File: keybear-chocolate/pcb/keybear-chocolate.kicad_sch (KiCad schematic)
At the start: 94 parts, among them J1 MJ-4PP-9, J3 LED, J4 OLED, P1 i2c-pin, P2 i2c-pin, SW1 SW_PUSH, SW10 SW_PUSH, SW11 SW_PUSH, SW12 SW_PUSH, SW13 SW_PUSH, SW14 SW_PUSH, SW15 SW_PUSH, SW16 SW_PUSH, SW17 SW_PUSH, SW18 SW_PUSH, SW19 SW_PUSH, SW2 SW_PUSH, SW20 SW_PUSH, SW21 SW_PUSH, SW22 SW_PUSH, SW23 SW_PUSH, SW25 Rotary_Encoder_Switch, SW3 SW_PUSH, SW4 SW_PUSH, SW5 SW_PUSH, SW6 SW_PUSH, SW7 SW_PUSH, SW8 SW_PUSH, SW9 SW_PUSH, U1 ProMicro

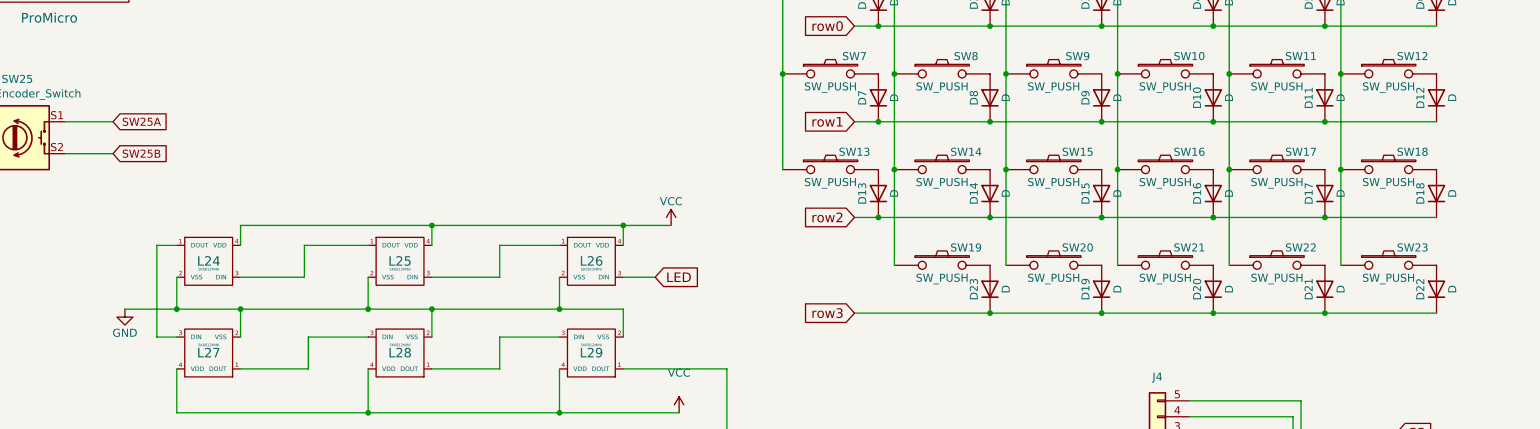
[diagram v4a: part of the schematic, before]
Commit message: rotary button mapped
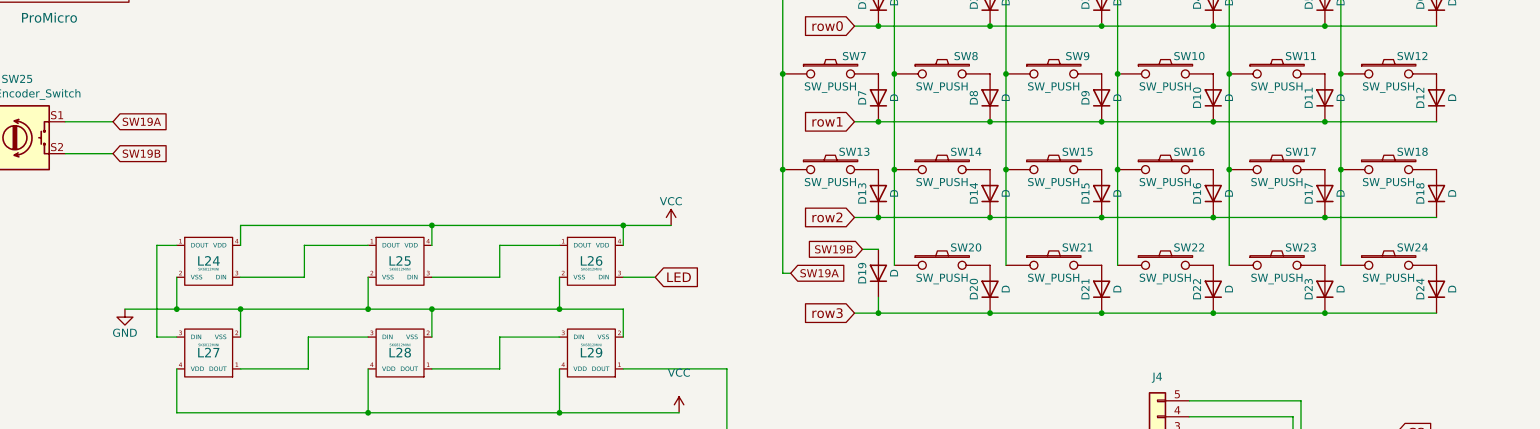
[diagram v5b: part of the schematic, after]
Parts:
- added D19: D, kbd:D3_SMD, symbol Device:D
- renumbered D23 to D20, D19 to D21, D20 to D22, D21 to D23, D22 to D24, SW19 to SW20, SW20 to SW21, SW21 to SW22, SW22 to SW23, SW23 to SW24
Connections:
- net col0 is gone; now on net SW19A: SW1.1, SW13.1, SW7.1, U1.20 (F4)
- net row3: now also D19.1 (K)
- net SW25A renamed SW19A
- net SW25B renamed SW19B
- net SW19B: now also D19.2 (A)
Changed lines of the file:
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@@
   (junction (at 250.19 104.14) (diameter 0) (color 0 0 0 0)
   )
+  (junction (at 179.07 104.14) (diameter 0) (color 0 0 0 0)
+  )
   (junction (at 196.85 73.66) (diameter 0) (color 0 0 0 0)
   )
@@
   (junction (at 200.66 151.765) (diameter 0) (color 0 0 0 0)
   )
+  (junction (at 163.83 81.28) (diameter 0) (color 0 0 0 0)
+  )
   (junction (at 107.95 103.505) (diameter 0) (color 0 0 0 0)
   )
@@
     (stroke (width 0) (type default))
   )
+  (wire (pts (xy 179.07 101.6) (xy 179.07 104.14))
+    (stroke (width 0) (type default))
+  )
   (wire (pts (xy 130.81 182.88) (xy 115.57 182.88))
     (stroke (width 0) (type default))
@@
     (stroke (width 0) (type default))
   )
+  (wire (pts (xy 163.83 97.79) (xy 163.83 81.28))
+    (stroke (width 0) (type default))
+  )
   (wire (pts (xy 74.93 173.99) (xy 74.93 170.18))
     (stroke (width 0) (type default))
@@
     (stroke (width 0) (type default))
   )
+  (wire (pts (xy 179.07 104.14) (xy 196.85 104.14))
+    (stroke (width 0) (type default))
+  )
   (wire (pts (xy 138.43 90.17) (xy 146.05 90.17))
     (stroke (width 0) (type default))
@@
     (stroke (width 0) (type default))
   )
-  (wire (pts (xy 175.26 104.14) (xy 196.85 104.14))
+  (wire (pts (xy 175.26 104.14) (xy 179.07 104.14))
     (stroke (width 0) (type default))
   )
@@
     (stroke (width 0) (type default))
   )
+  (wire (pts (xy 165.1 97.79) (xy 163.83 97.79))
+    (stroke (width 0) (type default))
+  )
   (wire (pts (xy 57.15 166.37) (xy 59.69 166.37))
     (stroke (width 0) (type default))
@@
     (stroke (width 0) (type default))
   )
+  (wire (pts (xy 176.53 93.98) (xy 179.07 93.98))
+    (stroke (width 0) (type default))
+  )
   (wire (pts (xy 77.47 113.03) (xy 88.265 113.03))
     (stroke (width 0) (type default))
@@
     )
   )
+  (global_label "SW19A" (shape input) (at 165.1 97.79 0)
+    (effects (font (size 1.27 1.27)) (justify left))
+    (property "Intersheetrefs" "${INTERSHEET_REFS}" (at 165.1 97.79 0)
+      (effects (font (size 1.27 1.27)) hide)
+    )
+  )
   (global_label "data" (shape input) (at 215.9 151.765 0) (fields_autoplaced)
     (effects (font (size 1.524 1.524)) (justify left))
@@
     )
   )
-  (global_label "SW25B" (shape input) (at 57.15 78.74 0)
+  (global_label "SW19B" (shape input) (at 57.15 78.74 0)
     (effects (font (size 1.27 1.27)) (justify left))
     (property "Intersheetrefs" "${INTERSHEET_REFS}" (at 57.15 78.74 0)
@@
     )
   )
+  (global_label "SW19B" (shape input) (at 176.53 93.98 180)
+    (effects (font (size 1.27 1.27)) (justify right))
+    (property "Intersheetrefs" "${INTERSHEET_REFS}" (at 176.53 93.98 0)
+      (effects (font (size 1.27 1.27)) hide)
+    )
+  )
   (global_label "ENCA" (shape input) (at 30.48 73.66 180)
     (effects (font (size 1.27 1.27)) (justify right))
@@
     )
   )
-  (global_label "SW25A" (shape input) (at 57.15 73.66 0)
+  (global_label "SW19A" (shape input) (at 57.15 73.66 0)
     (effects (font (size 1.27 1.27)) (justify left))
     (property "Intersheetrefs" "${INTERSHEET_REFS}" (at 57.15 73.66 0)
@@
   (symbol (lib_id "corne-chocolate-rescue:SW_PUSH-kbd") (at 242.57 96.52 0) (unit 1)
     (in_bom yes) (on_board yes) (dnp no)
-    (property "Reference" "SW22" (at 246.38 93.726 0)
+    (property "Reference" "SW23" (at 246.38 93.726 0)
       (effects (font (size 1.27 1.27)))
     )
@@
       (project "keybear-chocolate"
         (path "/b2404ab0-025a-473e-9fbb-0abc932972cf"
-          (reference "SW22") (unit 1)
+          (reference "SW23") (unit 1)
         )
       )
@@
   (symbol (lib_id "Device:D") (at 250.19 100.33 90) (unit 1)
     (in_bom yes) (on_board yes) (dnp no)
-    (property "Reference" "D21" (at 247.65 100.33 0)
+    (property "Reference" "D23" (at 247.65 100.33 0)
       (effects (font (size 1.27 1.27)))
     )
@@
       (project "keybear-chocolate"
         (path "/b2404ab0-025a-473e-9fbb-0abc932972cf"
-          (reference "D21") (unit 1)
+          (reference "D23") (unit 1)
         )
       )
@@
   (symbol (lib_id "corne-chocolate-rescue:SW_PUSH-kbd") (at 260.35 96.52 0) (unit 1)
     (in_bom yes) (on_board yes) (dnp no)
-    (property "Reference" "SW23" (at 264.16 93.726 0)
+    (property "Reference" "SW24" (at 264.16 93.726 0)
       (effects (font (size 1.27 1.27)))
     )
@@
       (project "keybear-chocolate"
         (path "/b2404ab0-025a-473e-9fbb-0abc932972cf"
-          (reference "SW23") (unit 1)
+          (reference "SW24") (unit 1)
         )
       )
@@
   (symbol (lib_id "Device:D") (at 267.97 100.33 90) (unit 1)
     (in_bom yes) (on_board yes) (dnp no)
-    (property "Reference" "D22" (at 265.43 100.33 0)
+    (property "Reference" "D24" (at 265.43 100.33 0)
       (effects (font (size 1.27 1.27)))
     )
@@
       (project "keybear-chocolate"
         (path "/b2404ab0-025a-473e-9fbb-0abc932972cf"
-          (reference "D22") (unit 1)
+          (reference "D24") (unit 1)
         )
       )
@@
   (symbol (lib_id "corne-chocolate-rescue:SW_PUSH-kbd") (at 224.79 96.52 0) (unit 1)
     (in_bom yes) (on_board yes) (dnp no)
-    (property "Reference" "SW21" (at 228.6 93.726 0)
+    (property "Reference" "SW22" (at 228.6 93.726 0)
       (effects (font (size 1.27 1.27)))
     )
@@
       (project "keybear-chocolate"
         (path "/b2404ab0-025a-473e-9fbb-0abc932972cf"
-          (reference "SW21") (unit 1)
+          (reference "SW22") (unit 1)
         )
       )
@@
   (symbol (lib_id "Device:D") (at 232.41 100.33 90) (unit 1)
     (in_bom yes) (on_board yes) (dnp no)
-    (property "Reference" "D20" (at 229.87 100.33 0)
+    (property "Reference" "D22" (at 229.87 100.33 0)
       (effects (font (size 1.27 1.27)))
     )
@@
       (project "keybear-chocolate"
         (path "/b2404ab0-025a-473e-9fbb-0abc932972cf"
-          (reference "D20") (unit 1)
+          (reference "D22") (unit 1)
         )
       )
@@
   (symbol (lib_id "corne-chocolate-rescue:SW_PUSH-kbd") (at 189.23 96.52 0) (unit 1)
     (in_bom yes) (on_board yes) (dnp no)
-    (property "Reference" "SW19" (at 193.04 93.726 0)
+    (property "Reference" "SW20" (at 193.04 93.726 0)
       (effects (font (size 1.27 1.27)))
     )
@@
       (project "keybear-chocolate"
         (path "/b2404ab0-025a-473e-9fbb-0abc932972cf"
-          (reference "SW19") (unit 1)
+          (reference "SW20") (unit 1)
         )
       )
@@
     )
   )
+  (symbol (lib_id "Device:D") (at 179.07 97.79 90) (unit 1)
+    (in_bom yes) (on_board yes) (dnp no)
+    (property "Reference" "D19" (at 176.53 97.79 0)
+      (effects (font (size 1.27 1.27)))
+    )
+    (property "Value" "D" (at 181.61 97.79 0)
+      (effects (font (size 1.27 1.27)))
+    )
+    (property "Footprint" "kbd:D3_SMD" (at 179.07 97.79 0)
+      (effects (font (size 1.27 1.27)) hide)
+    )
+    (property "Datasheet" "" (at 179.07 97.79 0)
+      (effects (font (size 1.27 1.27)) hide)
+    )
+    (pin "1")
+    (pin "2")
+    (instances
+      (project "keybear-chocolate"
+        (path "/b2404ab0-025a-473e-9fbb-0abc932972cf"
+          (reference "D19") (unit 1)
+        )
+      )
+    )
+  )
   (symbol (lib_id "SofleKeyboard-rescue:Rotary_Encoder_Switch-Device") (at 41.91 76.2 0) (unit 1)
     (in_bom yes) (on_board yes) (dnp no)
@@
   (symbol (lib_id "Device:D") (at 214.63 100.33 90) (unit 1)
     (in_bom yes) (on_board yes) (dnp no)
-    (property "Reference" "D19" (at 212.09 100.33 0)
+    (property "Reference" "D21" (at 212.09 100.33 0)
       (effects (font (size 1.27 1.27)))
     )
@@
       (project "keybear-chocolate"
         (path "/b2404ab0-025a-473e-9fbb-0abc932972cf"
-          (reference "D19") (unit 1)
+          (reference "D21") (unit 1)
         )
       )
@@
   (symbol (lib_id "corne-chocolate-rescue:SW_PUSH-kbd") (at 207.01 96.52 0) (unit 1)
     (in_bom yes) (on_board yes) (dnp no)
-    (property "Reference" "SW20" (at 210.82 93.726 0)
+    (property "Reference" "SW21" (at 210.82 93.726 0)
       (effects (font (size 1.27 1.27)))
     )
@@
       (project "keybear-chocolate"
         (path "/b2404ab0-025a-473e-9fbb-0abc932972cf"
-          (reference "SW20") (unit 1)
+          (reference "SW21") (unit 1)
         )
       )
@@
   (symbol (lib_id "Device:D") (at 196.85 100.33 90) (unit 1)
     (in_bom yes) (on_board yes) (dnp no)
-    (property "Reference" "D23" (at 194.31 100.33 0)
+    (property "Reference" "D20" (at 194.31 100.33 0)
       (effects (font (size 1.27 1.27)))
     )
@@
       (project "keybear-chocolate"
         (path "/b2404ab0-025a-473e-9fbb-0abc932972cf"
-          (reference "D23") (unit 1)
+          (reference "D20") (unit 1)
         )
       )

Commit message: latest schematics
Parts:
- added J2: BATT, kbd:StripLED_rev, symbol Connector_Generic:Conn_01x02
- added SW30: BATT_SW, Button_Switch_SMD:SW_SPDT_PCM12, symbol Switch:SW_SPDT
- SW1, SW2, SW3, SW4, SW5, SW6: footprint SofleChoc:Choc_Hotswap_SK6812MiniE -> kbd:Choc_Hotswap
- renumbered L19 to L20, L20 to L21, L21 to L22, L22 to L23, L23 to L24, L24 to L25, L25 to L26, L26 to L27, L27 to L28, L28 to L29, L29 to L30
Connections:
- net GND: now also J2.1 (Pin_1)
- net RAW: now reaches U1.24 (RAW)
- net RAW: now also SW30.1 (A)
- new net BATT_VCC: J2.2 (Pin_2), SW30.2 (B)

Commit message: using custom footprints
using custom footprints for leds and oled display
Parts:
- J4: footprint kbd:OLED -> kbd:OLED_xo_5pins
- L1, L10, L11, L12, L13, L14, L15, L16, L17, L18, L2, L20, L21, L22, L23, L24, L25, L26, L27, L28, L29, L3, L30, L4, L5, L6, L7, L8, L9: footprint kbd:SK6812MINI_rev -> kbd:SK6812MINI_xo_rev
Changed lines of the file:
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@@
       (effects (font (size 0.4064 0.4064)))
     )
-    (property "Footprint" "kbd:SK6812MINI_rev" (at 80.01 138.43 0)
+    (property "Footprint" "kbd:SK6812MINI_xo_rev" (at 80.01 138.43 0)
       (effects (font (size 1.524 1.524)) hide)
     )
@@
       (effects (font (size 0.4064 0.4064)))
     )
-    (property "Footprint" "kbd:SK6812MINI_rev" (at 95.25 138.43 0)
+    (property "Footprint" "kbd:SK6812MINI_xo_rev" (at 95.25 138.43 0)
       (effects (font (size 1.524 1.524)) hide)
     )
@@
       (effects (font (size 0.4064 0.4064)))
     )
-    (property "Footprint" "kbd:SK6812MINI_rev" (at 110.49 138.43 0)
+    (property "Footprint" "kbd:SK6812MINI_xo_rev" (at 110.49 138.43 0)
       (effects (font (size 1.524 1.524)) hide)
     )
@@
       (effects (font (size 0.4064 0.4064)))
     )
-    (property "Footprint" "kbd:SK6812MINI_rev" (at 125.73 138.43 0)
+    (property "Footprint" "kbd:SK6812MINI_xo_rev" (at 125.73 138.43 0)
       (effects (font (size 1.524 1.524)) hide)
     )
@@
       (effects (font (size 0.4064 0.4064)))
     )
-    (property "Footprint" "kbd:SK6812MINI_rev" (at 140.97 138.43 0)
+    (property "Footprint" "kbd:SK6812MINI_xo_rev" (at 140.97 138.43 0)
       (effects (font (size 1.524 1.524)) hide)
     )
@@
       (effects (font (size 0.4064 0.4064)))
     )
-    (property "Footprint" "kbd:SK6812MINI_rev" (at 64.77 138.43 0)
+    (property "Footprint" "kbd:SK6812MINI_xo_rev" (at 64.77 138.43 0)
       (effects (font (size 1.524 1.524)) hide)
     )
@@
       (effects (font (size 0.4064 0.4064)))
     )
-    (property "Footprint" "kbd:SK6812MINI_rev" (at 80.01 151.13 0)
+    (property "Footprint" "kbd:SK6812MINI_xo_rev" (at 80.01 151.13 0)
       (effects (font (size 1.524 1.524)) hide)
     )
@@
       (effects (font (size 0.4064 0.4064)))
     )
-    (property "Footprint" "kbd:SK6812MINI_rev" (at 95.25 151.13 0)
+    (property "Footprint" "kbd:SK6812MINI_xo_rev" (at 95.25 151.13 0)
       (effects (font (size 1.524 1.524)) hide)
     )
@@
       (effects (font (size 0.4064 0.4064)))
     )
-    (property "Footprint" "kbd:SK6812MINI_rev" (at 110.49 151.13 0)
+    (property "Footprint" "kbd:SK6812MINI_xo_rev" (at 110.49 151.13 0)
       (effects (font (size 1.524 1.524)) hide)
     )
@@
       (effects (font (size 0.4064 0.4064)))
     )
-    (property "Footprint" "kbd:SK6812MINI_rev" (at 125.73 151.13 0)
+    (property "Footprint" "kbd:SK6812MINI_xo_rev" (at 125.73 151.13 0)
       (effects (font (size 1.524 1.524)) hide)
     )
@@
       (effects (font (size 0.4064 0.4064)))
     )
-    (property "Footprint" "kbd:SK6812MINI_rev" (at 140.97 151.13 0)
+    (property "Footprint" "kbd:SK6812MINI_xo_rev" (at 140.97 151.13 0)
       (effects (font (size 1.524 1.524)) hide)
     )
@@
       (effects (font (size 0.4064 0.4064)))
     )
-    (property "Footprint" "kbd:SK6812MINI_rev" (at 64.77 151.13 0)
+    (property "Footprint" "kbd:SK6812MINI_xo_rev" (at 64.77 151.13 0)
       (effects (font (size 1.524 1.524)) hide)
     )
@@
       (effects (font (size 0.4064 0.4064)))
     )
-    (property "Footprint" "kbd:SK6812MINI_rev" (at 80.01 163.83 0)
+    (property "Footprint" "kbd:SK6812MINI_xo_rev" (at 80.01 163.83 0)
       (effects (font (size 1.524 1.524)) hide)
     )
@@
       (effects (font (size 0.4064 0.4064)))
     )
-    (property "Footprint" "kbd:SK6812MINI_rev" (at 95.25 163.83 0)
+    (property "Footprint" "kbd:SK6812MINI_xo_rev" (at 95.25 163.83 0)
       (effects (font (size 1.524 1.524)) hide)
     )
@@
       (effects (font (size 0.4064 0.4064)))
     )
-    (property "Footprint" "kbd:SK6812MINI_rev" (at 110.49 163.83 0)
+    (property "Footprint" "kbd:SK6812MINI_xo_rev" (at 110.49 163.83 0)
       (effects (font (size 1.524 1.524)) hide)
     )
@@
       (effects (font (size 0.4064 0.4064)))
     )
-    (property "Footprint" "kbd:SK6812MINI_rev" (at 125.73 163.83 0)
+    (property "Footprint" "kbd:SK6812MINI_xo_rev" (at 125.73 163.83 0)
       (effects (font (size 1.524 1.524)) hide)
     )
@@
       (effects (font (size 0.4064 0.4064)))
     )
-    (property "Footprint" "kbd:SK6812MINI_rev" (at 140.97 163.83 0)
+    (property "Footprint" "kbd:SK6812MINI_xo_rev" (at 140.97 163.83 0)
       (effects (font (size 1.524 1.524)) hide)
     )
@@
       (effects (font (size 0.4064 0.4064)))
     )
-    (property "Footprint" "kbd:SK6812MINI_rev" (at 64.77 163.83 0)
+    (property "Footprint" "kbd:SK6812MINI_xo_rev" (at 64.77 163.83 0)
       (effects (font (size 1.524 1.524)) hide)
     )
@@
       (effects (font (size 0.4064 0.4064)))
     )
-    (property "Footprint" "kbd:SK6812MINI_rev" (at 125.73 176.53 0)
+    (property "Footprint" "kbd:SK6812MINI_xo_rev" (at 125.73 176.53 0)
       (effects (font (size 1.524 1.524)) hide)
     )
@@
       (effects (font (size 0.4064 0.4064)))
     )
-    (property "Footprint" "kbd:SK6812MINI_rev" (at 140.97 176.53 0)
+    (property "Footprint" "kbd:SK6812MINI_xo_rev" (at 140.97 176.53 0)
       (effects (font (size 1.524 1.524)) hide)
     )
@@
       (effects (font (size 0.4064 0.4064)))
     )
-    (property "Footprint" "kbd:SK6812MINI_rev" (at 110.49 176.53 0)
+    (property "Footprint" "kbd:SK6812MINI_xo_rev" (at 110.49 176.53 0)
       (effects (font (size 1.524 1.524)) hide)
     )
@@
       (effects (font (size 0.4064 0.4064)))
     )
-    (property "Footprint" "kbd:SK6812MINI_rev" (at 133.35 95.885 0)
+    (property "Footprint" "kbd:SK6812MINI_xo_rev" (at 133.35 95.885 0)
       (effects (font (size 1.524 1.524)) hide)
     )
@@
       (effects (font (size 0.4064 0.4064)))
     )
-    (property "Footprint" "kbd:SK6812MINI_rev" (at 102.87 95.885 0)
+    (property "Footprint" "kbd:SK6812MINI_xo_rev" (at 102.87 95.885 0)
       (effects (font (size 1.524 1.524)) hide)
     )
@@
       (effects (font (size 0.4064 0.4064)))
     )
-    (property "Footprint" "kbd:SK6812MINI_rev" (at 72.39 95.885 0)
+    (property "Footprint" "kbd:SK6812MINI_xo_rev" (at 72.39 95.885 0)
       (effects (font (size 1.524 1.524)) hide)
     )
@@
       (effects (font (size 0.4064 0.4064)))
     )
-    (property "Footprint" "kbd:SK6812MINI_rev" (at 133.35 110.49 0)
+    (property "Footprint" "kbd:SK6812MINI_xo_rev" (at 133.35 110.49 0)
       (effects (font (size 1.524 1.524)) hide)
     )
@@
       (effects (font (size 0.4064 0.4064)))
     )
-    (property "Footprint" "kbd:SK6812MINI_rev" (at 102.87 110.49 0)
+    (property "Footprint" "kbd:SK6812MINI_xo_rev" (at 102.87 110.49 0)
       (effects (font (size 1.524 1.524)) hide)
     )
@@
       (effects (font (size 0.4064 0.4064)))
     )
-    (property "Footprint" "kbd:SK6812MINI_rev" (at 72.39 110.49 0)
+    (property "Footprint" "kbd:SK6812MINI_xo_rev" (at 72.39 110.49 0)
       (effects (font (size 1.524 1.524)) hide)
     )
@@
       (effects (font (size 0.4064 0.4064)))
     )
-    (property "Footprint" "kbd:SK6812MINI_rev" (at 80.01 176.53 0)
+    (property "Footprint" "kbd:SK6812MINI_xo_rev" (at 80.01 176.53 0)
       (effects (font (size 1.524 1.524)) hide)
     )
@@
       (effects (font (size 0.4064 0.4064)))
     )
-    (property "Footprint" "kbd:SK6812MINI_rev" (at 95.25 176.53 0)
+    (property "Footprint" "kbd:SK6812MINI_xo_rev" (at 95.25 176.53 0)
       (effects (font (size 1.524 1.524)) hide)
     )
@@
       (effects (font (size 1.27 1.27)))
     )
-    (property "Footprint" "kbd:OLED" (at 223.52 123.19 0)
-      (effects (font (size 1.27 1.27)) hide)
-    )
+    (property "Footprint" "kbd:OLED_xo_5pins" (at 223.52 123.19 0)
+      (effects (font (size 1.27 1.27)) hide)
+    )

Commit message: custom promicro added
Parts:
- U1: footprint kbd:ProMicro_v2 -> kbd:ProMicro_xo_1side
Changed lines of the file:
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@@
       (effects (font (size 1.524 1.524)))
     )
-    (property "Footprint" "kbd:ProMicro_v2" (at 49.53 69.85 0)
+    (property "Footprint" "kbd:ProMicro_xo_1side" (at 49.53 69.85 0)
       (effects (font (size 1.524 1.524)) hide)
     )
